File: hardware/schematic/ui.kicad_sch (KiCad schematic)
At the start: 15 parts, among them J2 Header 1x04 P2.54 H3.0 (OLED), SW2 EC11E18244A5, SW3 BTN1, SW4 BTN2

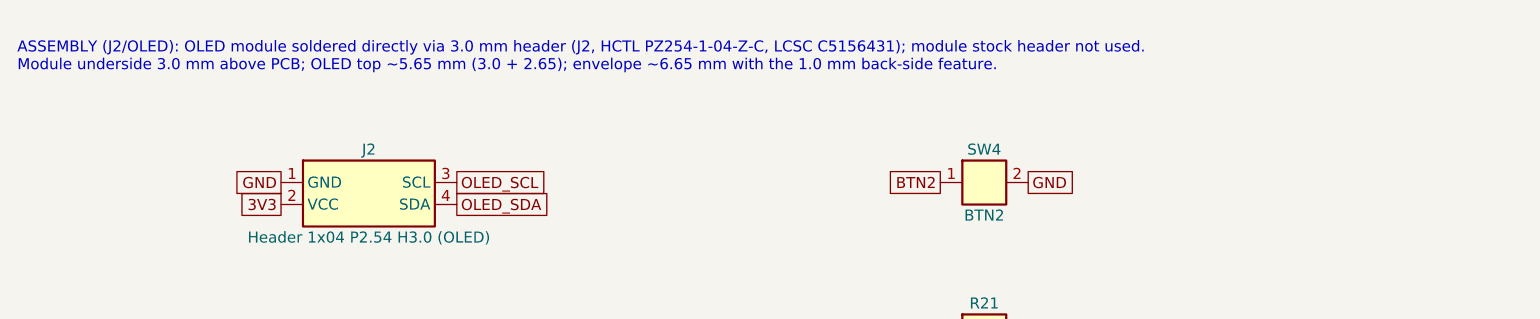
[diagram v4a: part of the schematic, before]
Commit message: OLED stack correction: OLED top ~5.65 mm, lowest point ~2.0 mm
PM correction: the earlier envelope figure double-counted the 1.0 mm
back feature. Stack above PCB top: module underside 3.0 mm; OLED top
~5.65 mm; lowest module point ~2.0 mm (1.0 mm back feature sits inside
the 3.0 mm gap). Added a first-build check: measure the module's actual
height above the PCB; if the header pin shoulder lifts it, update the
CAD height parameter.

- HAND EDIT (scripted): replaced the string of the ui-sheet assembly
  note (user-kicad has no text edit tool); position/size/uuid unchanged.
- docs/decisions.md: 'OLED mounting and stack (issue #44)' row updated.
run_erc: 0 violations.

Fixes #44
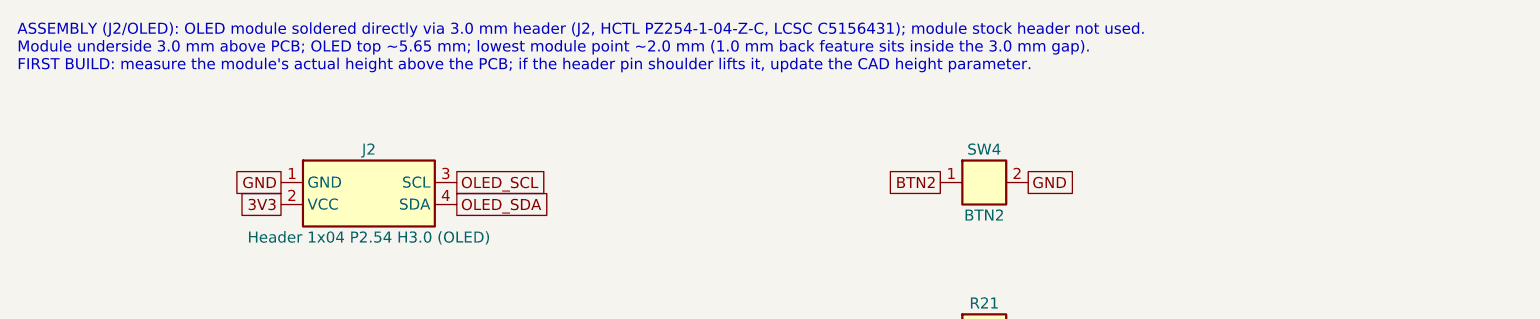
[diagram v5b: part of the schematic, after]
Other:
- note added: "ASSEMBLY (J2/OLED): OLED module soldered directly via 3.0 mm header (J2, HCTL PZ254-1-04-Z-C, LCSC C5156431); module stock header not used. Module underside 3.0 mm above PCB; OLED top ~5.65 mm; lowest module point ~2.0 mm (1.0 mm back feature sits inside the 3.0 mm gap). FIRST BUILD: measure the module's actual height above the PCB; if the header pin shoulder lifts it, update the CAD height param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"
- note removed: "ASSEMBLY (J2/OLED): OLED module soldered directly via 3.0 mm header (J2, HCTL PZ254-1-04-Z-C, LCSC C5156431); module stock header not used. Module underside 3.0 mm above PCB; OLED top ~5.65 mm (3.0 + 2.65); envelope ~6.65 mm with the 1.0 mm back-side feature."
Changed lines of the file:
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@@
 (global_label "LED_A" (shape passive) (at 132.08 73.66 180) (fields_autoplaced yes) (effects (font (size 1.27 1.27)) (justify right)) (property "Intersheetrefs" "${INTERSHEET_REFS}" (at 132.08 73.66 0) (effects (font (size 1.27 1.27)) (hide yes))))
 (global_label "GND" (shape passive) (at 147.32 73.66 0) (fields_autoplaced yes) (effects (font (size 1.27 1.27)) (justify left)) (property "Intersheetrefs" "${INTERSHEET_REFS}" (at 147.32 73.66 0) (effects (font (size 1.27 1.27)) (hide yes))))
-	(text "ASSEMBLY (J2/OLED): OLED module soldered directly via 3.0 mm header (J2, HCTL PZ254-1-04-Z-C, LCSC C5156431); module stock header not used.\nModule underside 3.0 mm above PCB; OLED top ~5.65 mm (3.0 + 2.65); envelope ~6.65 mm with the 1.0 mm back-side feature."
+	(text "ASSEMBLY (J2/OLED): OLED module soldered directly via 3.0 mm header (J2, HCTL PZ254-1-04-Z-C, LCSC C5156431); module stock header not used.\nModule underside 3.0 mm above PCB; OLED top ~5.65 mm; lowest module point ~2.0 mm (1.0 mm back feature sits inside the 3.0 mm gap).\nFIRST BUILD: measure the module's actual height above the PCB; if the header pin shoulder lifts it, update the CAD height parameter."
 		(exclude_from_sim no)
 		(at 25.4 25.4 0)
